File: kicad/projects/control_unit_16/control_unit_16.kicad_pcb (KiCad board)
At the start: 2 copper layers, 203.2 x 97.8 mm, 57 parts, among them J1 Conn_01x04_Female, J2 Control_signal_backplane, J3 Bus_connection, J4 Aux_connection, J5 Conn_01x16_Female, J6 LED_CONTROL, J7 TOP_POWER, U1 74HC04, U10 28C256, U11 28C256, U2 28C256, U3 74HC173, U4 74HC377, U5 74HC161, U6 28C256, U7 74HC245, U8 74HC245, U9 74HC138

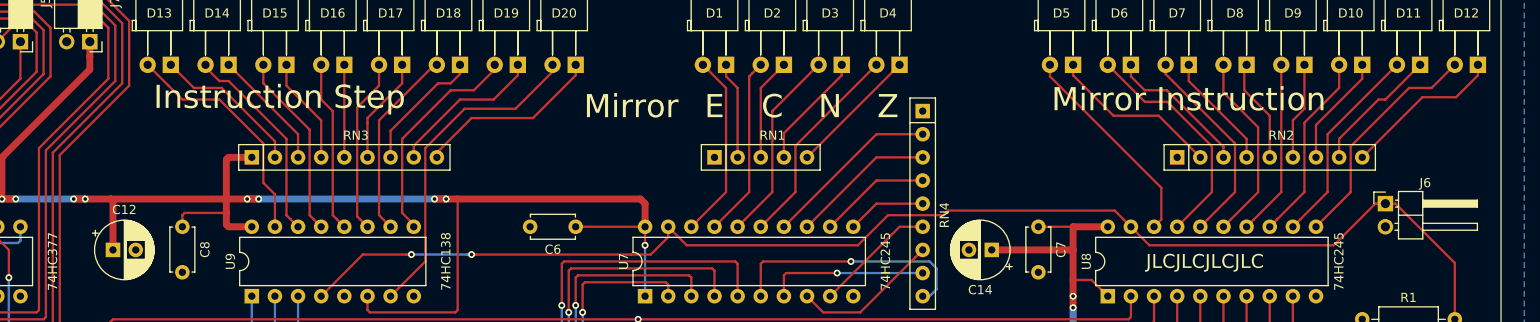
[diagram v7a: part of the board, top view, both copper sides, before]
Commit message: Add better labels to top power and LED control.
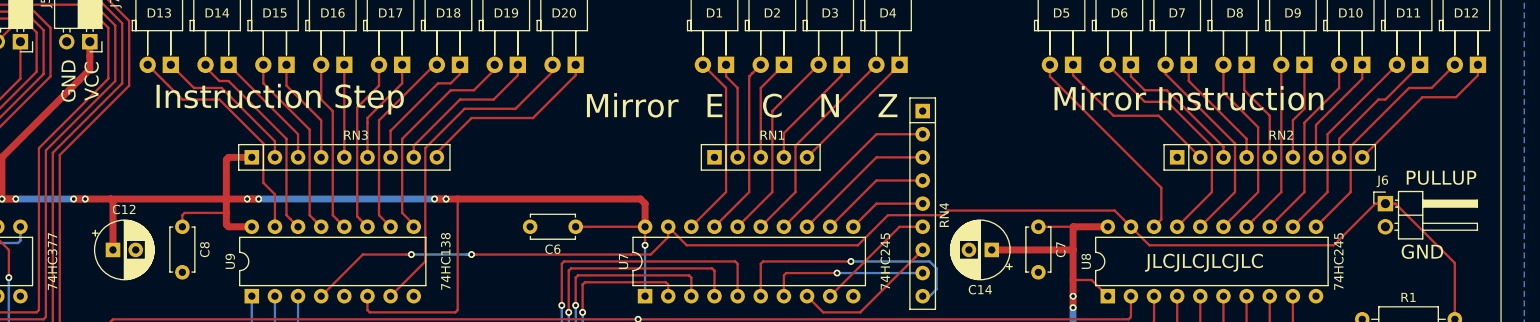
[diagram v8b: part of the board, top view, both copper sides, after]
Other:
- board text added: "GND"
- board text added: "PULLUP"
- board text added: "VCC"
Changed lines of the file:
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@@
   (general
     (thickness 1.6)
-    (drawings 40)
+    (drawings 44)
     (tracks 1317)
     (zones 0)
@@
     (descr "Through hole angled pin header, 1x02, 2.54mm pitch, 6mm pin length, single row")
     (tags "Through hole angled pin header THT 1x02 2.54mm single row")
-    (fp_text reference J6 (at 4.385 -2.27) (layer F.SilkS)
+    (fp_text reference J6 (at -0.254 -2.54) (layer F.SilkS)
       (effects (font (size 1 1) (thickness 0.15)))
     )
@@
     )
   )
+  (gr_text PULLUP (at 247.396 75.946) (layer F.SilkS)
+    (effects (font (size 1.524 1.524) (thickness 0.254)))
+  )
+  (gr_text GND (at 245.364 84.074) (layer F.SilkS)
+    (effects (font (size 1.524 1.524) (thickness 0.254)))
+  )
+  (gr_text GND (at 96.774 65.278 90) (layer F.SilkS)
+    (effects (font (size 1.524 1.524) (thickness 0.254)))
+  )
+  (gr_text VCC (at 99.314 65.278 90) (layer F.SilkS)
+    (effects (font (size 1.524 1.524) (thickness 0.254)))
+  )
   (gr_text "ROM 3" (at 167.132 101.346) (layer F.SilkS)
